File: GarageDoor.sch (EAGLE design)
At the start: 26 parts, among them IC1 7805DT, J1 DCJ0202

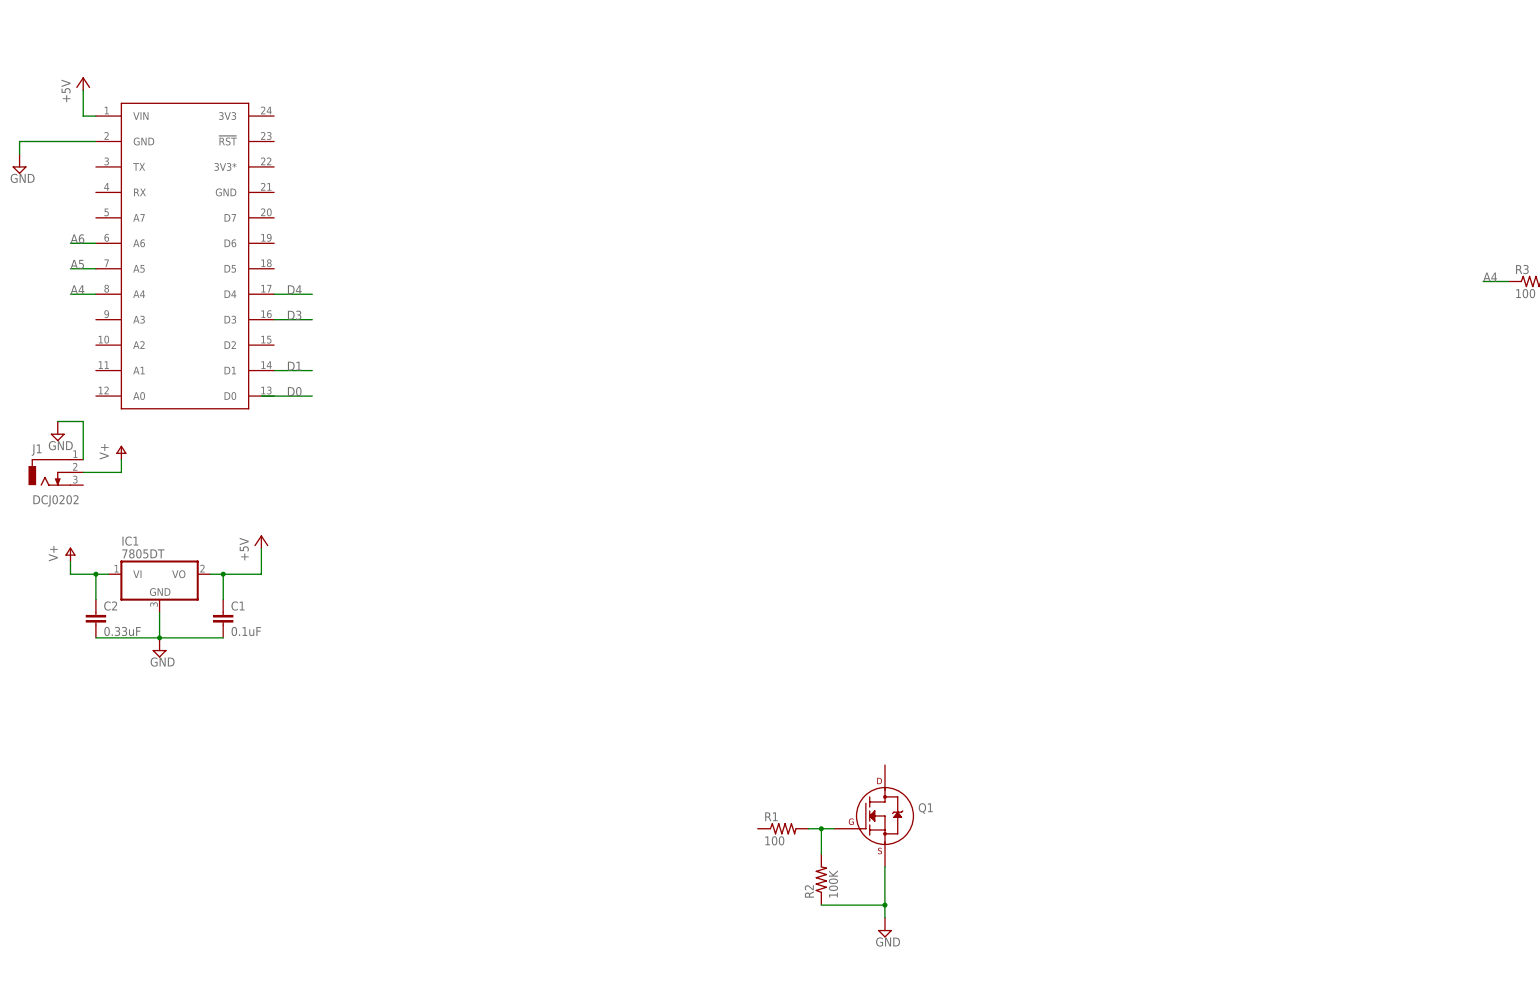
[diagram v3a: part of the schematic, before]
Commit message: Added Alarm and Hold
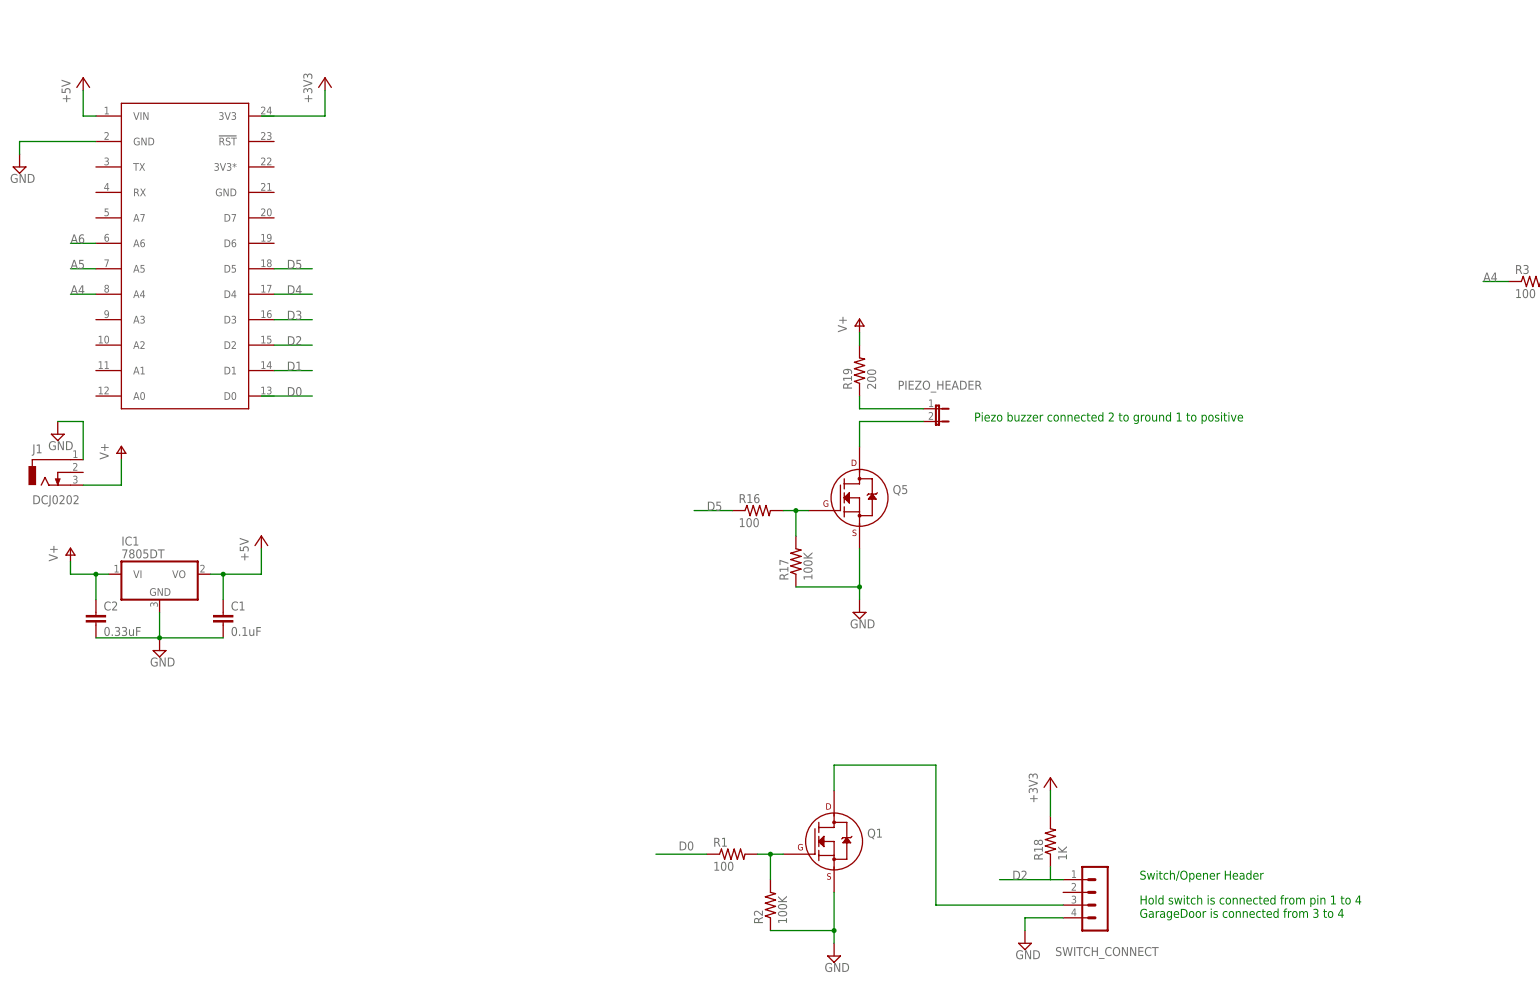
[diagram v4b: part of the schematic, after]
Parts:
- added PIEZO_HEADER: (no value), jumper:JP1E
- added Q5: (no value), transistors:2N7000_SOT23
- added R16: 100, resistor:R-US_R0805
- added R17: 100K, resistor:R-US_R0805
- added R18: 1K, resistor:R-US_R0805
- added R19: 200, resistor:R-US_R0805
- added SWITCH_CONNECT: (no value), con-lstb:MA04-1
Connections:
- new net +3V3: R18.2
- new net D0: R1.1
- new net D2: R18.1, SWITCH_CONNECT.1, U$1.D2
- new net D5: R16.1, U$1.D5
- new net N$14: Q5.G, R16.2, R17.2
- new net N$16: Q1.D, SWITCH_CONNECT.3
- new net N$17: PIEZO_HEADER.2, Q5.D
- new net N$18: PIEZO_HEADER.1, R19.1
- net GND: now also Q5.S, R17.1, SWITCH_CONNECT.4
- net V+: now also J1.3, R19.2; no longer J1.2
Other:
- note added: "Hold switch is connected from pin 1 to 4 GarageDoor is connected from 3 to 4"
- note added: "Piezo buzzer connected 2 to ground 1 to positive"
- note added: "Switch/Opener Header"
- moved on the sheet: Q1, R1, R2
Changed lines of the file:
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@@
 <part name="P+7" library="supply1" deviceset="+5V" device=""/>
 <part name="P+8" library="supply1" deviceset="+5V" device=""/>
+<part name="Q5" library="transistors" deviceset="2N700*" device="_SOT23" technology="0"/>
+<part name="R16" library="resistor" deviceset="R-US_" device="R0805" value="100"/>
+<part name="R17" library="resistor" deviceset="R-US_" device="R0805" value="100K"/>
+<part name="SUPPLY9" library="supply2" deviceset="GND" device=""/>
+<part name="SWITCH_CONNECT" library="con-lstb" deviceset="MA04-1" device=""/>
+<part name="SUPPLY10" library="supply2" deviceset="GND" device=""/>
+<part name="+3V1" library="supply1" deviceset="+3V3" device=""/>
+<part name="+3V2" library="supply1" deviceset="+3V3" device=""/>
+<part name="R18" library="resistor" deviceset="R-US_" device="R0805" value="1K"/>
+<part name="PIEZO_HEADER" library="jumper" deviceset="JP1E" device=""/>
+<part name="P+9" library="supply1" deviceset="V+" device=""/>
+<part name="R19" library="resistor" deviceset="R-US_" device="R0805" value="200"/>
 </parts>
 <sheets>
@@
 <text x="233.68" y="20.32" size="1.778" layer="91">D3 Is the Closed Detector
 D4 is the Opened Detector</text>
+<text x="86.36" y="-10.16" size="1.778" layer="91">Switch/Opener Header</text>
+<text x="86.36" y="-17.78" size="1.778" layer="91">Hold switch is connected from pin 1 to 4
+GarageDoor is connected from 3 to 4</text>
+<text x="53.34" y="81.28" size="1.778" layer="91">Piezo buzzer connected 2 to ground 1 to positive</text>
 </plain>
 <instances>
-<instance part="Q1" gate="G$1" x="35.56" y="2.54"/>
-<instance part="R1" gate="G$1" x="15.24" y="0"/>
-<instance part="R2" gate="G$1" x="22.86" y="-10.16" rot="R90"/>
+<instance part="Q1" gate="G$1" x="25.4" y="-2.54"/>
+<instance part="R1" gate="G$1" x="5.08" y="-5.08"/>
+<instance part="R2" gate="G$1" x="12.7" y="-15.24" rot="R90"/>
 <instance part="U$1" gate="G$1" x="-104.14" y="114.3"/>
 <instance part="Q2" gate="G$1" x="182.88" y="111.76"/>
@@
 <instance part="LED_RGB" gate="1" x="213.36" y="154.94" rot="R270"/>
 <instance part="P+1" gate="1" x="198.12" y="162.56"/>
-<instance part="SUPPLY5" gate="GND" x="35.56" y="-20.32"/>
+<instance part="SUPPLY5" gate="GND" x="25.4" y="-25.4"/>
 <instance part="HALL_CONN" gate="1" x="228.6" y="27.94" rot="R180"/>
 <instance part="P+2" gate="1" x="213.36" y="38.1"/>
@@
 <instance part="P+7" gate="1" x="205.74" y="53.34"/>
 <instance part="P+8" gate="1" x="203.2" y="22.86"/>
+<instance part="Q5" gate="G$1" x="30.48" y="66.04"/>
+<instance part="R16" gate="G$1" x="10.16" y="63.5"/>
+<instance part="R17" gate="G$1" x="17.78" y="53.34" rot="R90"/>
+<instance part="SUPPLY9" gate="GND" x="30.48" y="43.18"/>
+<instance part="SWITCH_CONNECT" gate="1" x="78.74" y="-15.24" smashed="yes" rot="R180">
+<attribute name="VALUE" x="80.01" y="-5.08" size="1.778" layer="96" rot="R180"/>
+<attribute name="NAME" x="90.17" y="-23.622" size="1.778" layer="95" rot="R180"/>
+</instance>
+<instance part="SUPPLY10" gate="GND" x="63.5" y="-22.86"/>
+<instance part="+3V1" gate="G$1" x="-76.2" y="149.86"/>
+<instance part="+3V2" gate="G$1" x="68.58" y="10.16"/>
+<instance part="R18" gate="G$1" x="68.58" y="-2.54" rot="R90"/>
+<instance part="PIEZO_HEADER" gate="A" x="45.72" y="83.82" smashed="yes" rot="R270">
+<attribute name="NAME" x="38.1" y="87.63" size="1.778" layer="95"/>
+<attribute name="VALUE" x="45.72" y="78.105" size="1.778" layer="96"/>
+</instance>
+<instance part="P+9" gate="1" x="30.48" y="101.6"/>
+<instance part="R19" gate="G$1" x="30.48" y="91.44" rot="R90"/>
 </instances>
 <busses>
@@
 <pinref part="R1" gate="G$1" pin="2"/>
 <pinref part="Q1" gate="G$1" pin="G"/>
-<wire x1="25.4" y1="0" x2="22.86" y2="0" width="0.1524" layer="91"/>
+<wire x1="15.24" y1="-5.08" x2="12.7" y2="-5.08" width="0.1524" layer="91"/>
 <pinref part="R2" gate="G$1" pin="2"/>
-<wire x1="22.86" y1="0" x2="20.32" y2="0" width="0.1524" layer="91"/>
-<wire x1="22.86" y1="-5.08" x2="22.86" y2="0" width="0.1524" layer="91"/>
-<junction x="22.86" y="0"/>
+<wire x1="12.7" y1="-5.08" x2="10.16" y2="-5.08" width="0.1524" layer="91"/>
+<wire x1="12.7" y1="-10.16" x2="12.7" y2="-5.08" width="0.1524" layer="91"/>
+<junction x="12.7" y="-5.08"/>
 </segment>
 </net>
@@
 <segment>
 <pinref part="Q1" gate="G$1" pin="S"/>
-<wire x1="35.56" y1="-7.62" x2="35.56" y2="-15.24" width="0.1524" layer="91"/>
+<wire x1="25.4" y1="-12.7" x2="25.4" y2="-20.32" width="0.1524" layer="91"/>
 <pinref part="R2" gate="G$1" pin="1"/>
-<wire x1="35.56" y1="-15.24" x2="35.56" y2="-17.78" width="0.1524" layer="91"/>
-<wire x1="22.86" y1="-15.24" x2="35.56" y2="-15.24" width="0.1524" layer="91"/>
-<junction x="35.56" y="-15.24"/>
+<wire x1="25.4" y1="-20.32" x2="25.4" y2="-22.86" width="0.1524" layer="91"/>
+<wire x1="12.7" y1="-20.32" x2="25.4" y2="-20.32" width="0.1524" layer="91"/>
+<junction x="25.4" y="-20.32"/>
 <pinref part="SUPPLY5" gate="GND" pin="GND"/>
 </segment>
@@
 <wire x1="-124.46" y1="81.28" x2="-129.54" y2="81.28" width="0.1524" layer="91"/>
 </segment>
+<segment>
+<pinref part="Q5" gate="G$1" pin="S"/>
+<wire x1="30.48" y1="55.88" x2="30.48" y2="48.26" width="0.1524" layer="91"/>
+<pinref part="R17" gate="G$1" pin="1"/>
+<wire x1="30.48" y1="48.26" x2="30.48" y2="45.72" width="0.1524" layer="91"/>
+<wire x1="17.78" y1="48.26" x2="30.48" y2="48.26" width="0.1524" layer="91"/>
+<junction x="30.48" y="48.26"/>
+<pinref part="SUPPLY9" gate="GND" pin="GND"/>
+</segment>
+<segment>
+<pinref part="SUPPLY10" gate="GND" pin="GND"/>
+<wire x1="71.12" y1="-17.78" x2="63.5" y2="-17.78" width="0.1524" layer="91"/>
+<wire x1="63.5" y1="-17.78" x2="63.5" y2="-20.32" width="0.1524" layer="91"/>
+<pinref part="SWITCH_CONNECT" gate="1" pin="4"/>
+</segment>
 </net>
 <net name="N$5" class="0">
@@
 <label x="-83.82" y="86.36" size="1.778" layer="95"/>
 </segment>
+<segment>
+<pinref part="R1" gate="G$1" pin="1"/>
+<wire x1="0" y1="-5.08" x2="-10.16" y2="-5.08" width="0.1524" layer="91"/>
+<label x="-2.54" y="-2.54" size="1.778" layer="95" rot="R180"/>
+</segment>
 </net>
 <net name="D1" class="0">
@@
 </segment>
 <segment>
-<pinref part="J1" gate="G$1" pin="2"/>
+<pinref part="P+9" gate="1" pin="V+"/>
+<pinref part="R19" gate="G$1" pin="2"/>
+<wire x1="30.48" y1="99.06" x2="30.48" y2="96.52" width="0.1524" layer="91"/>
+</segment>
+<segment>
+<pinref part="J1" gate="G$1" pin="3"/>
 <pinref part="P+5" gate="1" pin="V+"/>
-<wire x1="-124.46" y1="71.12" x2="-116.84" y2="71.12" width="0.1524" layer="91"/>
-<wire x1="-116.84" y1="71.12" x2="-116.84" y2="73.66" width="0.1524" layer="91"/>
+<wire x1="-124.46" y1="68.58" x2="-116.84" y2="68.58" width="0.1524" layer="91"/>
+<wire x1="-116.84" y1="68.58" x2="-116.84" y2="73.66" width="0.1524" layer="91"/>
 </segment>
 </net>
@@
 </segment>
 </net>
+<net name="N$14" class="0">
+<segment>
+<pinref part="R16" gate="G$1" pin="2"/>
+<pinref part="Q5" gate="G$1" pin="G"/>
+<wire x1="20.32" y1="63.5" x2="17.78" y2="63.5" width="0.1524" layer="91"/>
+<pinref part="R17" gate="G$1" pin="2"/>
+<wire x1="17.78" y1="63.5" x2="15.24" y2="63.5" width="0.1524" layer="91"/>
+<wire x1="17.78" y1="58.42" x2="17.78" y2="63.5" width="0.1524" layer="91"/>
+<junction x="17.78" y="63.5"/>
+</segment>
+</net>
+<net name="+3V3" class="0">
+<segment>
+<pinref part="R18" gate="G$1" pin="2"/>
+<pinref part="+3V2" gate="G$1" pin="+3V3"/>
+<wire x1="68.58" y1="2.54" x2="68.58" y2="7.62" width="0.1524" layer="91"/>
+</segment>
+<segment>
+<pinref part="+3V1" gate="G$1" pin="+3V3"/>
+<wire x1="-88.9" y1="142.24" x2="-76.2" y2="142.24" width="0.1524" layer="91"/>
+<wire x1="-76.2" y1="142.24" x2="-76.2" y2="147.32" width="0.1524" layer="91"/>
+</segment>
+</net>
+<net name="D5" class="0">
+<segment>
+<pinref part="U$1" gate="G$1" pin="D5"/>
+<wire x1="-86.36" y1="111.76" x2="-78.74" y2="111.76" width="0.1524" layer="91"/>
+<label x="-83.82" y="111.76" size="1.778" layer="95"/>
+</segment>
+<segment>
+<pinref part="R16" gate="G$1" pin="1"/>
+<wire x1="5.08" y1="63.5" x2="-2.54" y2="63.5" width="0.1524" layer="91"/>
+<label x="0" y="63.5" size="1.778" layer="95"/>
+</segment>
+</net>
+<net name="D2" class="0">
+<segment>
+<pinref part="SWITCH_CONNECT" gate="1" pin="1"/>
+<wire x1="71.12" y1="-10.16" x2="68.58" y2="-10.16" width="0.1524" layer="91"/>
+<pinref part="R18" gate="G$1" pin="1"/>
+<wire x1="58.42" y1="-10.16" x2="68.58" y2="-10.16" width="0.1524" layer="91"/>
+<wire x1="68.58" y1="-10.16" x2="68.58" y2="-7.62" width="0.1524" layer="91"/>
+<label x="60.96" y="-10.16" size="1.778" layer="95"/>
+</segment>
+<segment>
+<pinref part="U$1" gate="G$1" pin="D2"/>
+<wire x1="-86.36" y1="96.52" x2="-78.74" y2="96.52" width="0.1524" layer="91"/>
+<label x="-83.82" y="96.52" size="1.778" layer="95"/>
+</segment>
+</net>
+<net name="N$16" class="0">
+<segment>
+<pinref part="Q1" gate="G$1" pin="D"/>
+<wire x1="25.4" y1="7.62" x2="25.4" y2="12.7" width="0.1524" layer="91"/>
+<wire x1="25.4" y1="12.7" x2="45.72" y2="12.7" width="0.1524" layer="91"/>
+<wire x1="45.72" y1="12.7" x2="45.72" y2="-15.24" width="0.1524" layer="91"/>
+<wire x1="45.72" y1="-15.24" x2="71.12" y2="-15.24" width="0.1524" layer="91"/>
+<pinref part="SWITCH_CONNECT" gate="1" pin="3"/>
+</segment>
+</net>
+<net name="N$17" class="0">
+<segment>
+<pinref part="Q5" gate="G$1" pin="D"/>
+<wire x1="30.48" y1="81.28" x2="30.48" y2="76.2" width="0.1524" layer="91"/>
+<wire x1="30.48" y1="81.28" x2="43.18" y2="81.28" width="0.1524" layer="91"/>
+<pinref part="PIEZO_HEADER" gate="A" pin="2"/>
+</segment>
+</net>
+<net name="N$18" class="0">
+<segment>
+<pinref part="R19" gate="G$1" pin="1"/>
+<wire x1="30.48" y1="86.36" x2="30.48" y2="83.82" width="0.1524" layer="91"/>
+<wire x1="30.48" y1="83.82" x2="43.18" y2="83.82" width="0.1524" layer="91"/>
+<pinref part="PIEZO_HEADER" gate="A" pin="1"/>
+</segment>
+</net>

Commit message: PIR
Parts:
- added PIR_HEADER: (no value), con-lstb:MA03-1
- added R20: 10K, resistor:R-US_R0805
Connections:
- new net A0: PIR_HEADER.3, R20.1, U$1.A0
- net +3V3: now also R20.2
- net +5V: now also PIR_HEADER.1
- net GND: now also PIR_HEADER.2
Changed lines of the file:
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@@
 <part name="P+9" library="supply1" deviceset="V+" device=""/>
 <part name="R19" library="resistor" deviceset="R-US_" device="R0805" value="200"/>
+<part name="PIR_HEADER" library="con-lstb" deviceset="MA03-1" device=""/>
+<part name="R20" library="resistor" deviceset="R-US_" device="R0805" value="10K"/>
+<part name="P+10" library="supply1" deviceset="+5V" device=""/>
+<part name="+3V3" library="supply1" deviceset="+3V3" device=""/>
+<part name="SUPPLY11" library="supply2" deviceset="GND" device=""/>
 </parts>
 <sheets>
@@
 <instance part="P+9" gate="1" x="30.48" y="101.6"/>
 <instance part="R19" gate="G$1" x="30.48" y="91.44" rot="R90"/>
+<instance part="PIR_HEADER" gate="G$1" x="50.8" y="129.54" rot="R180"/>
+<instance part="R20" gate="G$1" x="25.4" y="129.54" rot="R90"/>
+<instance part="P+10" gate="1" x="40.64" y="139.7"/>
+<instance part="+3V3" gate="G$1" x="25.4" y="139.7"/>
+<instance part="SUPPLY11" gate="GND" x="33.02" y="132.08"/>
 </instances>
 <busses>
@@
 <pinref part="SWITCH_CONNECT" gate="1" pin="4"/>
 </segment>
+<segment>
+<pinref part="PIR_HEADER" gate="G$1" pin="2"/>
+<wire x1="43.18" y1="129.54" x2="38.1" y2="129.54" width="0.1524" layer="91"/>
+<wire x1="38.1" y1="129.54" x2="38.1" y2="134.62" width="0.1524" layer="91"/>
+<pinref part="SUPPLY11" gate="GND" pin="GND"/>
+<wire x1="38.1" y1="134.62" x2="33.02" y2="134.62" width="0.1524" layer="91"/>
+</segment>
 </net>
 <net name="N$5" class="0">
@@
 <pinref part="P+8" gate="1" pin="+5V"/>
 <wire x1="203.2" y1="17.78" x2="203.2" y2="20.32" width="0.1524" layer="91"/>
+</segment>
+<segment>
+<pinref part="PIR_HEADER" gate="G$1" pin="1"/>
+<pinref part="P+10" gate="1" pin="+5V"/>
+<wire x1="43.18" y1="132.08" x2="40.64" y2="132.08" width="0.1524" layer="91"/>
+<wire x1="40.64" y1="132.08" x2="40.64" y2="137.16" width="0.1524" layer="91"/>
 </segment>
 </net>
@@
 <wire x1="-76.2" y1="142.24" x2="-76.2" y2="147.32" width="0.1524" layer="91"/>
 </segment>
+<segment>
+<pinref part="R20" gate="G$1" pin="2"/>
+<pinref part="+3V3" gate="G$1" pin="+3V3"/>
+<wire x1="25.4" y1="134.62" x2="25.4" y2="137.16" width="0.1524" layer="91"/>
+</segment>
 </net>
 <net name="D5" class="0">
@@
 </segment>
 </net>
+<net name="A0" class="0">
+<segment>
+<pinref part="U$1" gate="G$1" pin="A0"/>
+<wire x1="-121.92" y1="86.36" x2="-127" y2="86.36" width="0.1524" layer="91"/>
+<label x="-127" y="86.36" size="1.778" layer="95"/>
+</segment>
+<segment>
+<pinref part="PIR_HEADER" gate="G$1" pin="3"/>
+<wire x1="43.18" y1="127" x2="33.02" y2="127" width="0.1524" layer="91"/>
+<wire x1="33.02" y1="127" x2="33.02" y2="124.46" width="0.1524" layer="91"/>
+<pinref part="R20" gate="G$1" pin="1"/>
+<wire x1="33.02" y1="124.46" x2="25.4" y2="124.46" width="0.1524" layer="91"/>
+<wire x1="25.4" y1="124.46" x2="17.78" y2="124.46" width="0.1524" layer="91"/>
+<junction x="25.4" y="124.46"/>
+<label x="17.78" y="124.46" size="1.778" layer="95"/>
+</segment>
+</net>
